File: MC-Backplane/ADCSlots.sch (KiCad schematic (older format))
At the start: 3 parts, among them J41 86094328314755V1LF, J42 86094328314755V1LF, J43 86094328314755V1LF

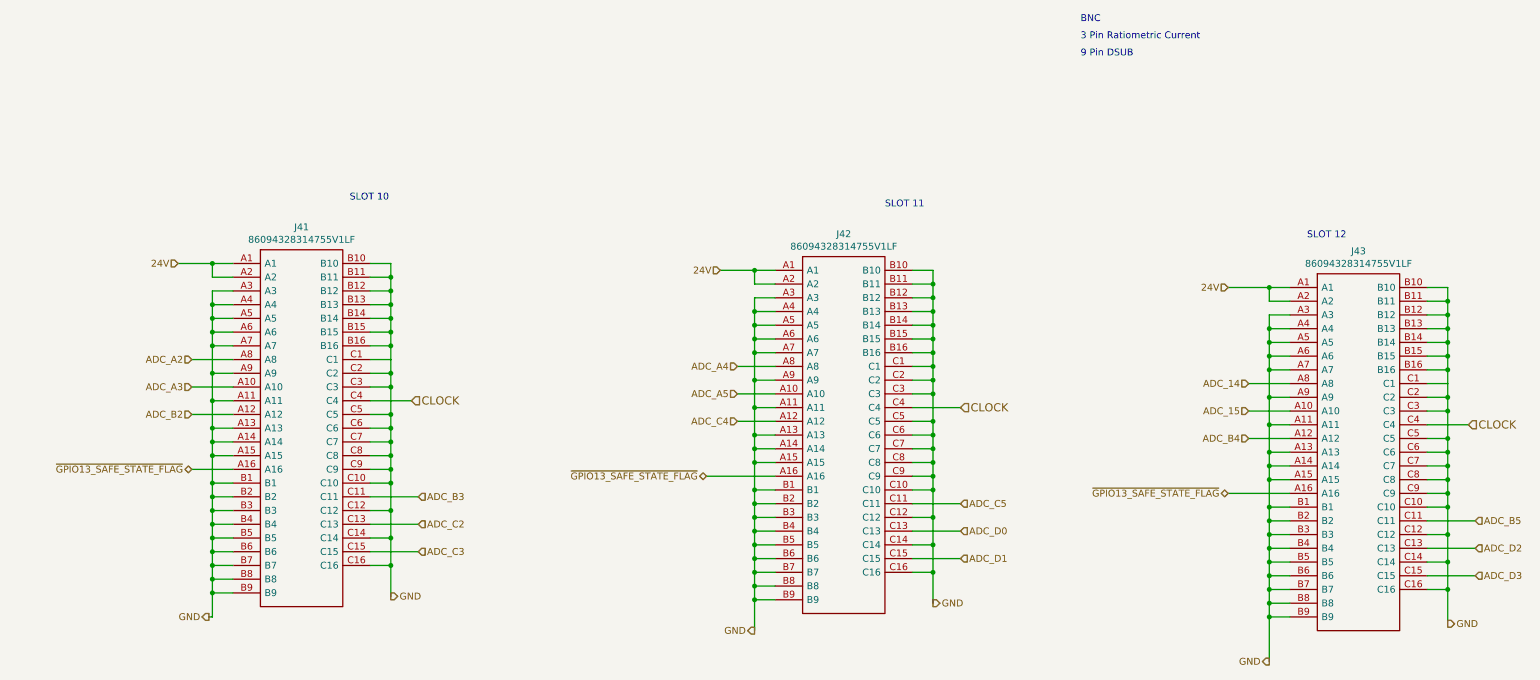
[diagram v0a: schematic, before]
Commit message: schematic reorg and layout begins
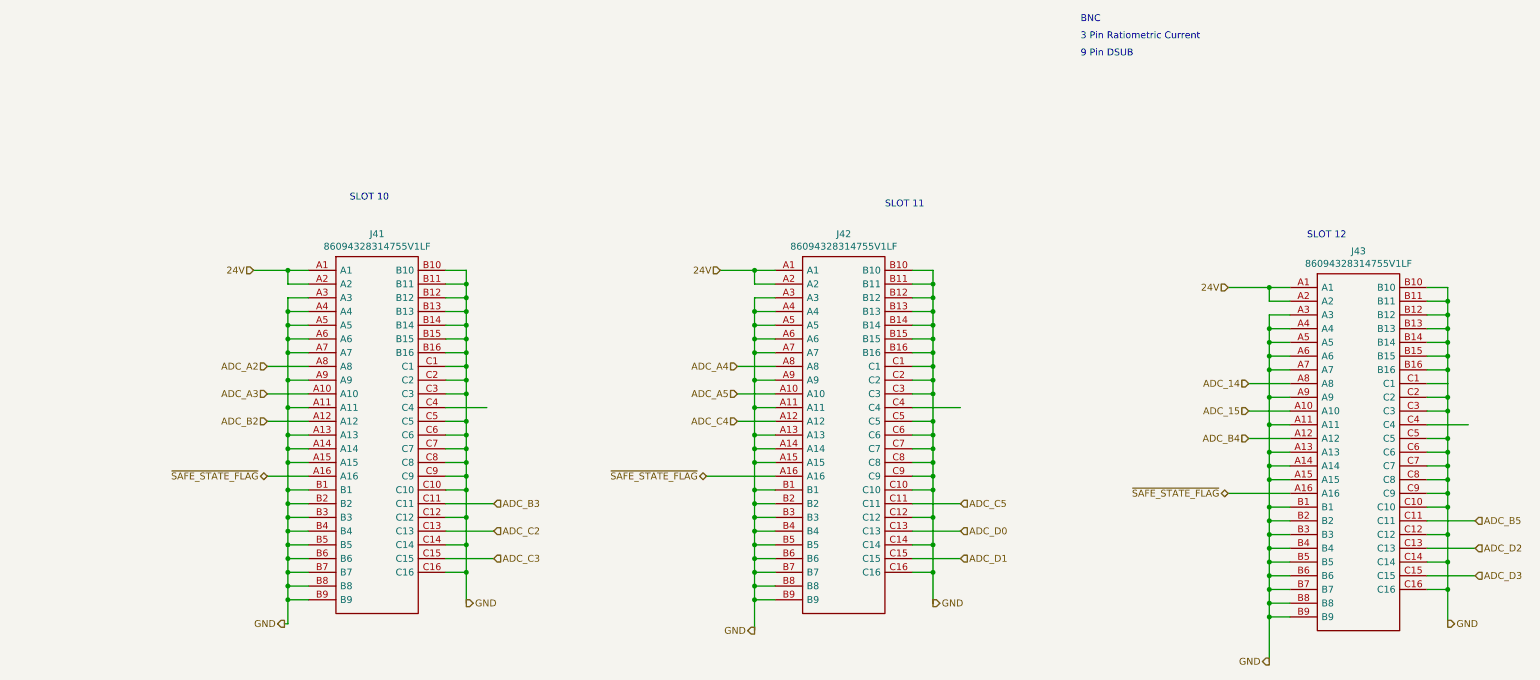
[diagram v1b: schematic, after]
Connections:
- net CLOCK: no longer names the net of J41.C4, J42.C4, J43.C4
- net ~GPIO13_SAFE_STATE_FLAG~ renamed ~SAFE_STATE_FLAG~
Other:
- moved on the sheet: J41
